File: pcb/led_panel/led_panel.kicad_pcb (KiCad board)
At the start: 2 copper layers, 160 x 41.1 mm, 62 parts

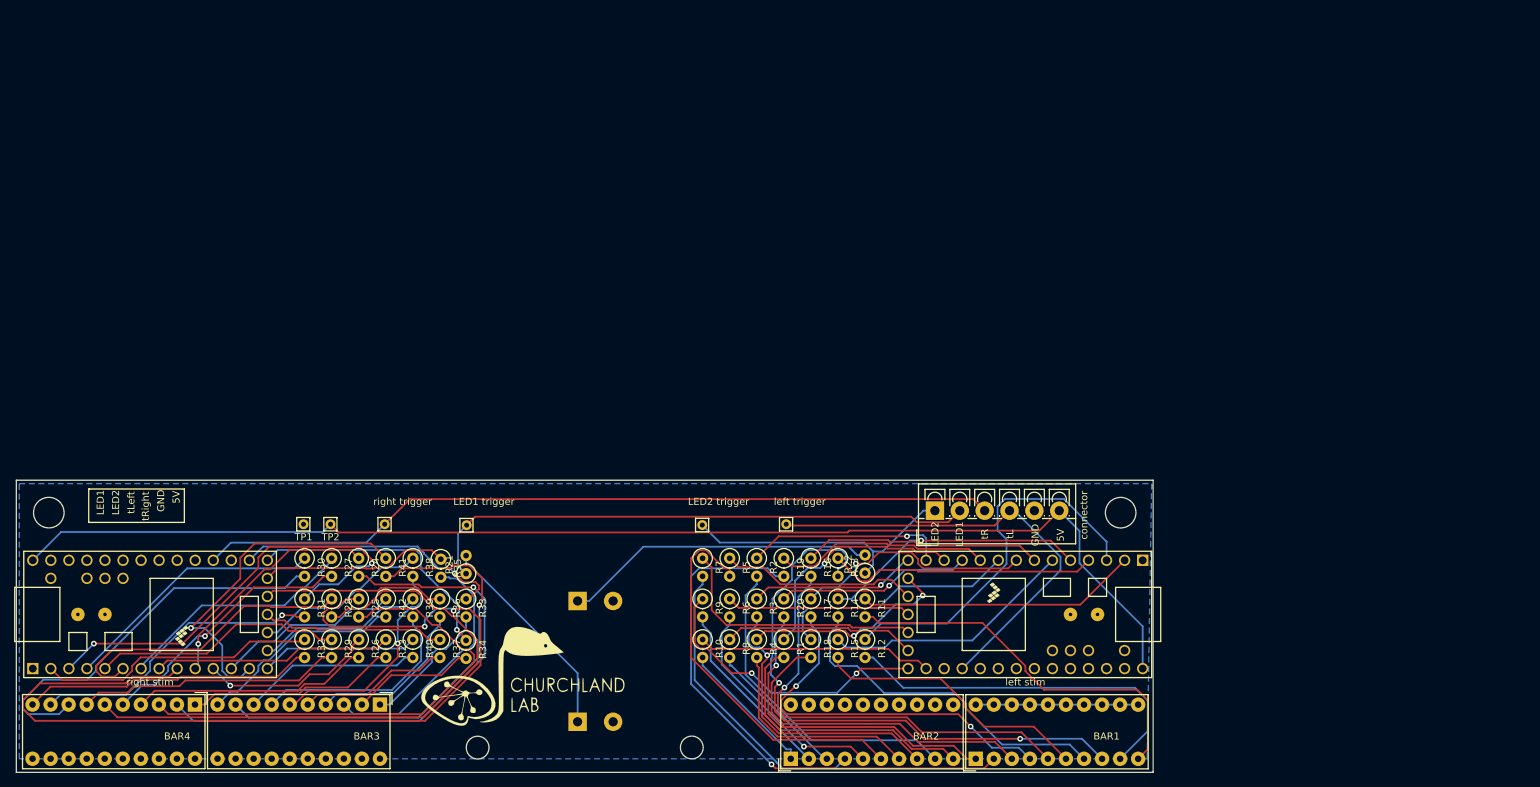
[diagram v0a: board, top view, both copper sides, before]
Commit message: Corrected LED panel pcb (teensy bug...)
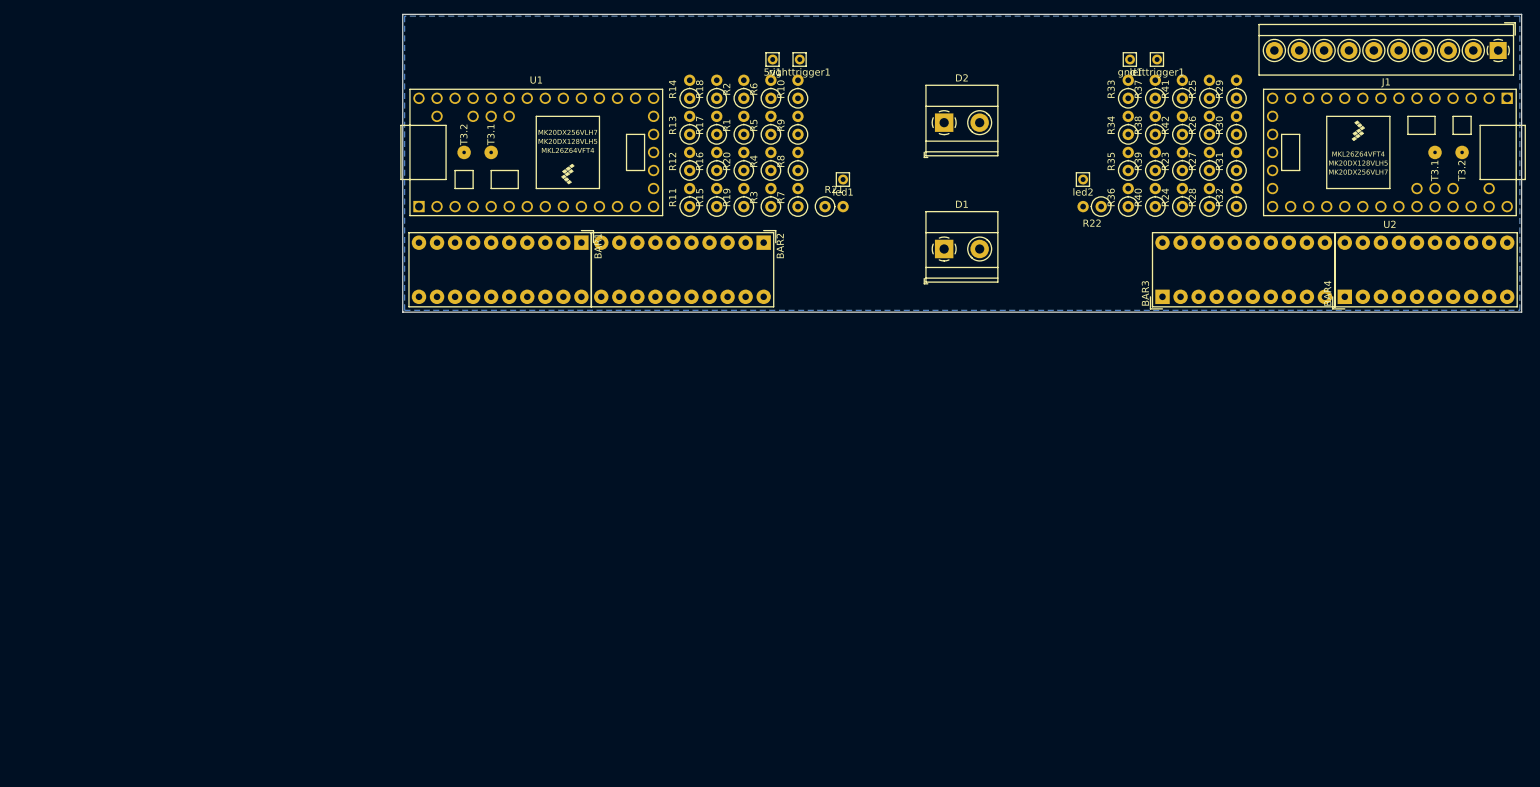
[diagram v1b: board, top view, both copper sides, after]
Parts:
- removed G***: LOGO, lib:churchland_lab_logo
- removed LED1: distractor LED 1, TerminalBlock_Phoenix:TerminalBlock_Phoenix_MKDS-1,5-2_1x02_P5.00mm_Horizontal
- removed LED1 trigger: LED1 trigger, Connector_Pin:Pin_D0.7mm_L6.5mm_W1.8mm_FlatFork
- removed LED2: distractor LED 2, TerminalBlock_Phoenix:TerminalBlock_Phoenix_MKDS-1,5-2_1x02_P5.00mm_Horizontal
- removed LED2 trigger: LED2 trigger, Connector_Pin:Pin_D0.7mm_L6.5mm_W1.8mm_FlatFork
- removed REF** (x2): MountingHole_3.2mm_M3, MountingHole:MountingHole_3.2mm_M3
- removed REF** (x2): MountingHole_4.3mm_M4, MountingHole:MountingHole_4.3mm_M4
- removed TP1: GND, Connector_Pin:Pin_D0.7mm_L6.5mm_W1.8mm_FlatFork
- removed TP2: 5V, Connector_Pin:Pin_D0.7mm_L6.5mm_W1.8mm_FlatFork
- removed connector: Screw_Terminal, TerminalBlock_4Ucon:TerminalBlock_4Ucon_1x06_P3.50mm_Vertical
- removed left stim: Teensy3.2, lib:Teensy30_31_32_LC
- removed left trigger: left trigger, Connector_Pin:Pin_D0.7mm_L6.5mm_W1.8mm_FlatFork
- removed right stim: Teensy3.2, lib:Teensy30_31_32_LC
- removed right trigger: right trigger, Connector_Pin:Pin_D0.7mm_L6.5mm_W1.8mm_FlatFork
- added 5v1: 5V, Connector_Pin:Pin_D0.7mm_L6.5mm_W1.8mm_FlatFork, F.Cu at (124.5, -29.2)
- added D1: LED, TerminalBlock_Phoenix:TerminalBlock_Phoenix_MKDS-1,5-2_1x02_P5.00mm_Horizontal, F.Cu at (148.6, -2.54)
- added D2: LED, TerminalBlock_Phoenix:TerminalBlock_Phoenix_MKDS-1,5-2_1x02_P5.00mm_Horizontal, F.Cu at (148.6, -20.3)
- added J1: Screw_Terminal_01x10, TerminalBlock_4Ucon:TerminalBlock_4Ucon_1x10_P3.50mm_Horizontal, F.Cu at (226.6, -30.5)
- added U1: Teensy3.2, lib:Teensy30_31_32_LC, F.Cu at (91.2, -16.1)
- added U2: Teensy3.2, lib:Teensy30_31_32_LC, F.Cu at (211.3, -16.1)
- added gnd1: GND, Connector_Pin:Pin_D0.7mm_L6.5mm_W1.8mm_FlatFork, F.Cu at (174.8, -29.2)
- added led1: LED1 test, Connector_Pin:Pin_D0.7mm_L6.5mm_W1.8mm_FlatFork, F.Cu at (134.4, -12.3)
- added led2: LED2 test, Connector_Pin:Pin_D0.7mm_L6.5mm_W1.8mm_FlatFork, F.Cu at (168.1, -12.3)
- added lefttrigger1: left trigger, Connector_Pin:Pin_D0.7mm_L6.5mm_W1.8mm_FlatFork, F.Cu at (178.6, -29.2)
- added righttrigger1: right trigger, Connector_Pin:Pin_D0.7mm_L6.5mm_W1.8mm_FlatFork, F.Cu at (128.3, -29.2)
- moved BAR4 171.7 mm to (205.0, 4.19), turned to 90 degrees
- moved R29 148.4 mm to (189.7, -23.7), turned to 90 degrees
- moved R32 144.6 mm to (189.7, -8.51), turned to 90 degrees
- moved R31 144.4 mm to (189.7, -13.6), turned to 90 degrees
- moved R30 144.1 mm to (189.7, -18.7), turned to 90 degrees
- moved R26 139.3 mm to (185.9, -18.7), turned to 90 degrees
- moved R25 138.9 mm to (185.9, -23.7), turned to 90 degrees
- moved R28 135.3 mm to (185.9, -8.51), turned to 90 degrees
- moved R27 135.1 mm to (185.9, -13.6), turned to 90 degrees
- moved R23 130.1 mm to (182.1, -13.6), turned to 90 degrees
- moved R42 129.8 mm to (182.1, -18.7), turned to 90 degrees
- moved R41 129.5 mm to (182.1, -23.7), turned to 90 degrees
- moved R37 126.3 mm to (178.3, -23.7), turned to 90 degrees
- moved R24 126.1 mm to (182.1, -8.51), turned to 90 degrees
- moved BAR3 124.2 mm to (179.3, 4.19), turned to 90 degrees
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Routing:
- net +5V: track 175.4 -> 0.00 mm
- net Net-(R25-Pad1): track 131.2 -> 0.00 mm, vias 2 -> 0
- net Net-(J1-Pad3): track 112.8 -> 0.00 mm
- net Net-(BAR4-Pad6): track 84.5 -> 0.00 mm
- net Net-(BAR1-Pad8): track 83.8 -> 0.00 mm, vias 2 -> 0
- net Net-(J1-Pad5): track 78.7 -> 0.00 mm
- net Net-(BAR1-Pad2): track 77.2 -> 0.00 mm, vias 1 -> 0
- net Net-(BAR4-Pad2): track 75.1 -> 0.00 mm, vias 1 -> 0
- net Net-(BAR4-Pad3): track 68.4 -> 0.00 mm
- net Net-(BAR3-Pad9): track 64.8 -> 0.00 mm, vias 1 -> 0
- net Net-(J1-Pad4): track 63.7 -> 0.00 mm
- net Net-(R31-Pad1): track 63.4 -> 0.00 mm, vias 2 -> 0
- net Net-(BAR1-Pad5): track 61.6 -> 0.00 mm, vias 1 -> 0
- net Net-(BAR4-Pad8): track 55.7 -> 0.00 mm
- net Net-(BAR2-Pad6): track 54.7 -> 0.00 mm
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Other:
- board size 160 x 41.1 mm -> 157.5 x 41.9 mm
- net class Default: trace_width 0.25 -> 0.3
- board text removed: "5V"
- board text removed: "GND"
- board text removed: "LED1"
- board text removed: "LED2"
- board text removed: "tL"
- board text removed: "tLeft"
- board text removed: "tR"
- board text removed: "tRight"

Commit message: LED panel layout before applying routing.
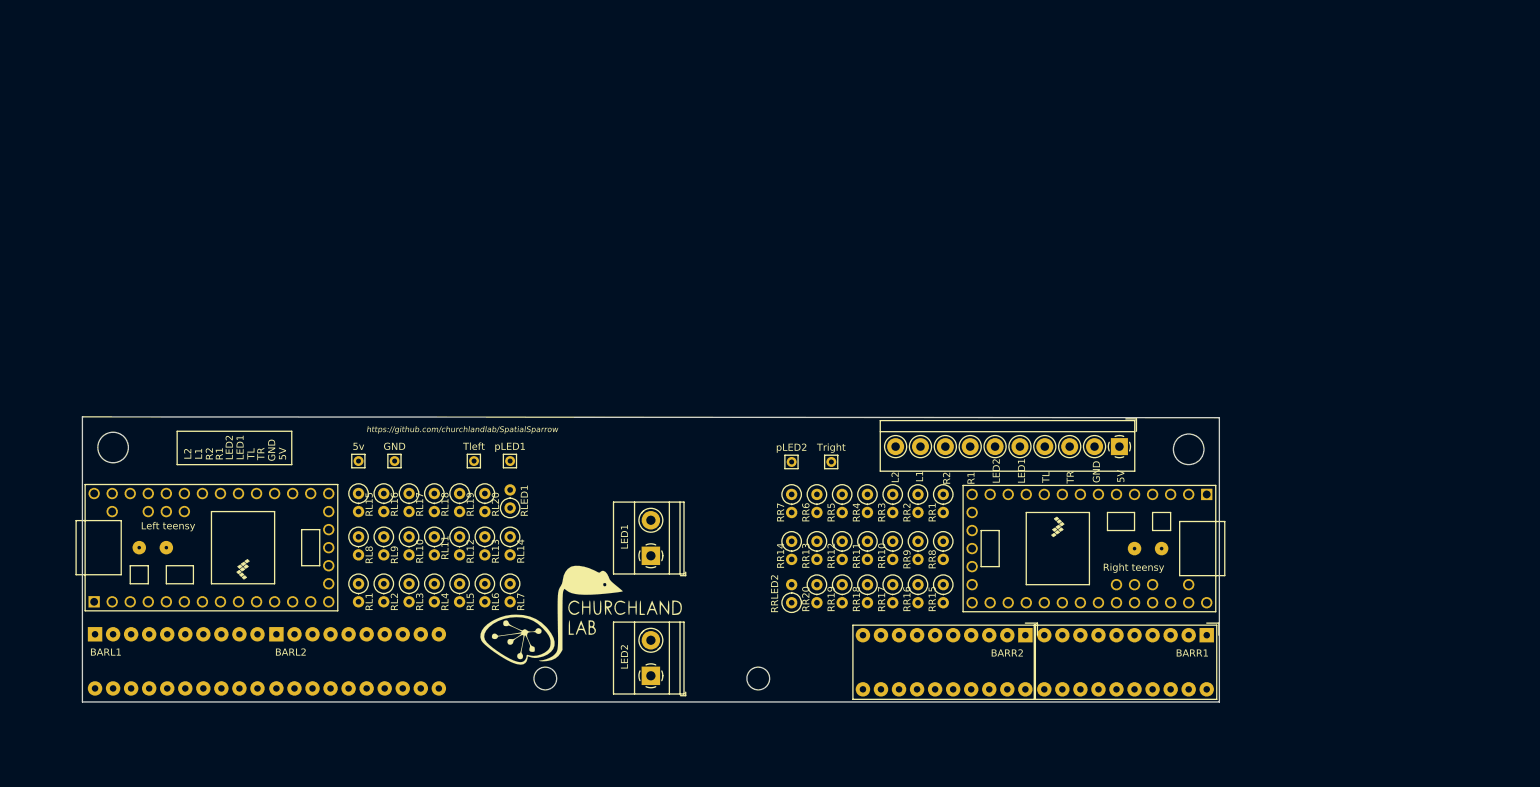
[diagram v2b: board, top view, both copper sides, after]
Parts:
- removed 5v1: 5V, Connector_Pin:Pin_D0.7mm_L6.5mm_W1.8mm_FlatFork
- removed BAR1, BAR2, BAR3, BAR4: HDSP-4830_2, Display:HDSP-4830
- removed D1, D2: LED, TerminalBlock_Phoenix:TerminalBlock_Phoenix_MKDS-1,5-2_1x02_P5.00mm_Horizontal
- removed J1: Screw_Terminal_01x10, TerminalBlock_4Ucon:TerminalBlock_4Ucon_1x10_P3.50mm_Horizontal
- removed R1, R10, R11, R12, R13, R14, R15, R16, R17, R18, R19, R2, R20, R21, R22, R23, R24, R25, R26, R27, R28, R29, R3, R30, R31, R32, R33, R34, R35, R36, R37, R38, R39, R4, R40, R41, R42, R5, R6, R7, R8, R9: R, Resistor_THT:R_Axial_DIN0207_L6.3mm_D2.5mm_P2.54mm_Vertical
- removed U1, U2: Teensy3.2, lib:Teensy30_31_32_LC
- removed gnd1: GND, Connector_Pin:Pin_D0.7mm_L6.5mm_W1.8mm_FlatFork
- removed led1: LED1 test, Connector_Pin:Pin_D0.7mm_L6.5mm_W1.8mm_FlatFork
- removed led2: LED2 test, Connector_Pin:Pin_D0.7mm_L6.5mm_W1.8mm_FlatFork
- removed lefttrigger1: left trigger, Connector_Pin:Pin_D0.7mm_L6.5mm_W1.8mm_FlatFork
- removed righttrigger1: right trigger, Connector_Pin:Pin_D0.7mm_L6.5mm_W1.8mm_FlatFork
- added 5v: 5V, Connector_Pin:Pin_D0.7mm_L6.5mm_W1.8mm_FlatFork, F.Cu at (66.2, 27.3)
- added BARL1: HDSP-4830_2, Display:HDSP-4830, B.Cu at (29.1, 51.7)
- added BARL2: HDSP-4830_2, Display:HDSP-4830, B.Cu at (54.6, 51.7)
- added BARR1: HDSP-4830_2, Display:HDSP-4830, F.Cu at (185.5, 51.8)
- added BARR2: HDSP-4830_2, Display:HDSP-4830, F.Cu at (160.0, 51.8)
- added G***: LOGO, lib:churchland_lab_logo, F.Cu at (98.0, 49.0)
- added GND: GND, Connector_Pin:Pin_D0.7mm_L6.5mm_W1.8mm_FlatFork, F.Cu at (71.2, 27.3)
- added LED1: LED, TerminalBlock_Phoenix:TerminalBlock_Phoenix_MKDS-1,5-2_1x02_P5.00mm_Horizontal, F.Cu at (107.3, 40.6)
- added LED2: LED, TerminalBlock_Phoenix:TerminalBlock_Phoenix_MKDS-1,5-2_1x02_P5.00mm_Horizontal, F.Cu at (107.3, 57.5)
- added Left teensy: Teensy3.2, lib:Teensy30_31_32_LC, F.Cu at (45.5, 39.5)
- added M3_1: MountingHole_3.2mm_M3, MountingHole:MountingHole_3.2mm_M3, F.Cu at (92.5, 57.9)
- added M3_2: MountingHole_3.2mm_M3, MountingHole:MountingHole_3.2mm_M3, F.Cu at (122.4, 57.9)
- added M4_1: MountingHole_4.3mm_M4, MountingHole:MountingHole_4.3mm_M4, F.Cu at (31.6, 25.4)
- added M4_2: MountingHole_4.3mm_M4, MountingHole:MountingHole_4.3mm_M4, F.Cu at (183.0, 25.7)
- added RL1: R, Resistor_THT:R_Axial_DIN0207_L6.3mm_D2.5mm_P2.54mm_Vertical, F.Cu at (66.2, 44.6)
- added RL10: R, Resistor_THT:R_Axial_DIN0207_L6.3mm_D2.5mm_P2.54mm_Vertical, F.Cu at (73.3, 38.0)
- added RL11: R, Resistor_THT:R_Axial_DIN0207_L6.3mm_D2.5mm_P2.54mm_Vertical, F.Cu at (76.8, 38.0)
- added RL12: R, Resistor_THT:R_Axial_DIN0207_L6.3mm_D2.5mm_P2.54mm_Vertical, F.Cu at (80.4, 38.0)
- added RL13: R, Resistor_THT:R_Axial_DIN0207_L6.3mm_D2.5mm_P2.54mm_Vertical, F.Cu at (83.9, 38.0)
- added RL14: R, Resistor_THT:R_Axial_DIN0207_L6.3mm_D2.5mm_P2.54mm_Vertical, F.Cu at (87.5, 38.0)
- added RL15: R, Resistor_THT:R_Axial_DIN0207_L6.3mm_D2.5mm_P2.54mm_Vertical, F.Cu at (66.2, 31.9)
- added RL16: R, Resistor_THT:R_Axial_DIN0207_L6.3mm_D2.5mm_P2.54mm_Vertical, F.Cu at (69.7, 31.9)
- added RL17: R, Resistor_THT:R_Axial_DIN0207_L6.3mm_D2.5mm_P2.54mm_Vertical, F.Cu at (73.3, 31.9)
- added RL18: R, Resistor_THT:R_Axial_DIN0207_L6.3mm_D2.5mm_P2.54mm_Vertical, F.Cu at (76.8, 31.9)
- added RL19: R, Resistor_THT:R_Axial_DIN0207_L6.3mm_D2.5mm_P2.54mm_Vertical, F.Cu at (80.4, 31.9)
- added RL2: R, Resistor_THT:R_Axial_DIN0207_L6.3mm_D2.5mm_P2.54mm_Vertical, F.Cu at (69.7, 44.6)
- added RL20: R, Resistor_THT:R_Axial_DIN0207_L6.3mm_D2.5mm_P2.54mm_Vertical, F.Cu at (83.9, 31.9)
- added RL3: R, Resistor_THT:R_Axial_DIN0207_L6.3mm_D2.5mm_P2.54mm_Vertical, F.Cu at (73.3, 44.6)
- added RL4: R, Resistor_THT:R_Axial_DIN0207_L6.3mm_D2.5mm_P2.54mm_Vertical, F.Cu at (76.8, 44.6)
- added RL5: R, Resistor_THT:R_Axial_DIN0207_L6.3mm_D2.5mm_P2.54mm_Vertical, F.Cu at (80.4, 44.6)
- added RL6: R, Resistor_THT:R_Axial_DIN0207_L6.3mm_D2.5mm_P2.54mm_Vertical, F.Cu at (83.9, 44.6)
- added RL7: R, Resistor_THT:R_Axial_DIN0207_L6.3mm_D2.5mm_P2.54mm_Vertical, F.Cu at (87.5, 44.6)
- added RL8: R, Resistor_THT:R_Axial_DIN0207_L6.3mm_D2.5mm_P2.54mm_Vertical, F.Cu at (66.2, 38.0)
- added RL9: R, Resistor_THT:R_Axial_DIN0207_L6.3mm_D2.5mm_P2.54mm_Vertical, F.Cu at (69.7, 38.0)
- added RLED1: R, Resistor_THT:R_Axial_DIN0207_L6.3mm_D2.5mm_P2.54mm_Vertical, F.Cu at (87.5, 33.9)
- added RR1: R, Resistor_THT:R_Axial_DIN0207_L6.3mm_D2.5mm_P2.54mm_Vertical, F.Cu at (148.5, 32.0)
- added RR10: R, Resistor_THT:R_Axial_DIN0207_L6.3mm_D2.5mm_P2.54mm_Vertical, F.Cu at (141.4, 38.6)
- added RR11: R, Resistor_THT:R_Axial_DIN0207_L6.3mm_D2.5mm_P2.54mm_Vertical, F.Cu at (137.8, 38.6)
- added RR12: R, Resistor_THT:R_Axial_DIN0207_L6.3mm_D2.5mm_P2.54mm_Vertical, F.Cu at (134.2, 38.6)
- added RR13: R, Resistor_THT:R_Axial_DIN0207_L6.3mm_D2.5mm_P2.54mm_Vertical, F.Cu at (130.7, 38.6)
- added RR14: R, Resistor_THT:R_Axial_DIN0207_L6.3mm_D2.5mm_P2.54mm_Vertical, F.Cu at (127.1, 38.6)
- added RR15: R, Resistor_THT:R_Axial_DIN0207_L6.3mm_D2.5mm_P2.54mm_Vertical, F.Cu at (148.5, 44.7)
- added RR16: R, Resistor_THT:R_Axial_DIN0207_L6.3mm_D2.5mm_P2.54mm_Vertical, F.Cu at (144.9, 44.7)
- added RR17: R, Resistor_THT:R_Axial_DIN0207_L6.3mm_D2.5mm_P2.54mm_Vertical, F.Cu at (141.4, 44.7)
- added RR18: R, Resistor_THT:R_Axial_DIN0207_L6.3mm_D2.5mm_P2.54mm_Vertical, F.Cu at (137.8, 44.7)
- added RR19: R, Resistor_THT:R_Axial_DIN0207_L6.3mm_D2.5mm_P2.54mm_Vertical, F.Cu at (134.2, 44.7)
- added RR2: R, Resistor_THT:R_Axial_DIN0207_L6.3mm_D2.5mm_P2.54mm_Vertical, F.Cu at (144.9, 32.0)
- added RR20: R, Resistor_THT:R_Axial_DIN0207_L6.3mm_D2.5mm_P2.54mm_Vertical, F.Cu at (130.7, 44.7)
- added RR3: R, Resistor_THT:R_Axial_DIN0207_L6.3mm_D2.5mm_P2.54mm_Vertical, F.Cu at (141.4, 32.0)
- added RR4: R, Resistor_THT:R_Axial_DIN0207_L6.3mm_D2.5mm_P2.54mm_Vertical, F.Cu at (137.8, 32.0)
- added RR5: R, Resistor_THT:R_Axial_DIN0207_L6.3mm_D2.5mm_P2.54mm_Vertical, F.Cu at (134.2, 32.0)
- added RR6: R, Resistor_THT:R_Axial_DIN0207_L6.3mm_D2.5mm_P2.54mm_Vertical, F.Cu at (130.7, 32.0)
- added RR7: R, Resistor_THT:R_Axial_DIN0207_L6.3mm_D2.5mm_P2.54mm_Vertical, F.Cu at (127.1, 32.0)
- added RR8: R, Resistor_THT:R_Axial_DIN0207_L6.3mm_D2.5mm_P2.54mm_Vertical, F.Cu at (148.5, 38.6)
- added RR9: R, Resistor_THT:R_Axial_DIN0207_L6.3mm_D2.5mm_P2.54mm_Vertical, F.Cu at (144.9, 38.6)
- added RRLED2: R, Resistor_THT:R_Axial_DIN0207_L6.3mm_D2.5mm_P2.54mm_Vertical, F.Cu at (127.1, 47.2)
- added Right teensy: Teensy3.2, lib:Teensy30_31_32_LC, F.Cu at (169.0, 39.6)
- added Tleft: T right, Connector_Pin:Pin_D0.7mm_L6.5mm_W1.8mm_FlatFork, F.Cu at (82.4, 27.3)
- added Tright: T right, Connector_Pin:Pin_D0.7mm_L6.5mm_W1.8mm_FlatFork, F.Cu at (132.7, 27.4)
- added pLED1: LED1, Connector_Pin:Pin_D0.7mm_L6.5mm_W1.8mm_FlatFork, F.Cu at (87.5, 27.3)
- added pLED2: LED2, Connector_Pin:Pin_D0.7mm_L6.5mm_W1.8mm_FlatFork, F.Cu at (127.1, 27.4)
- added terminal: Screw_Terminal_01x10, TerminalBlock_4Ucon:TerminalBlock_4Ucon_1x10_P3.50mm_Horizontal, F.Cu at (173.3, 25.3)
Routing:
- removed copper zone on B.Cu, net GND
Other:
- board size 157.5 x 41.9 mm -> 160 x 40.1 mm
- board text added: "5V"
- board text added: "GND"
- board text added: "L1"
- board text added: "L2"
- board text added: "LED1"
- board text added: "LED2"
- board text added: "R1"
- board text added: "R2"
- board text added: "TL"
- board text added: "TR"
- board text added: "https://github.com/churchlandlab/SpatialSparrow"

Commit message: Routed LED panel
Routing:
- net GND: track 0.00 -> 243.4 mm
- net +5V: track 0.00 -> 176.0 mm
- net Net-(J1-Pad4): track 0.00 -> 130.2 mm
- net Net-(J1-Pad9): track 0.00 -> 107.2 mm
- net Net-(J1-Pad10): track 0.00 -> 105.4 mm
- net Net-(BARR1-Pad3): track 0.00 -> 84.4 mm
- net Net-(D1-Pad2): track 0.00 -> 79.9 mm
- net Net-(J1-Pad3): track 0.00 -> 73.6 mm
- net Net-(RR20-Pad1): track 0.00 -> 70.1 mm, vias 0 -> 1
- net Net-(BARL1-Pad8): track 0.00 -> 67.1 mm
- net Net-(BARR1-Pad6): track 0.00 -> 66.2 mm, vias 0 -> 1
- net Net-(D2-Pad2): track 0.00 -> 63.6 mm
- net Net-(BARR1-Pad7): track 0.00 -> 58.5 mm
- net Net-(BARL1-Pad9): track 0.00 -> 55.7 mm, vias 0 -> 1
- net Net-(BARL1-Pad10): track 0.00 -> 55.0 mm
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- added copper zone on F.Cu, net +5V
- added copper zone on B.Cu, net GND
